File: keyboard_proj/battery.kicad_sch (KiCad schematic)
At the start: 11 parts

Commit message: Tous les schematics vérifiés 1x
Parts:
- removed Q?: FS8205A, SOP65P640X120-8N, symbol SamacSys_Parts:FS8205A
- removed R?: 1k, symbol Device:R
- added BatteryConnector: Conn_01x02, symbol Connector_Generic:Conn_01x02
- added Q?: FS8205A, SOT-23-6L_TCP, symbol 2024-04-15_18-05-36:FS8205A
- added R?: 1k, symbol Device:R
- gave numbers to parts that had none: 2
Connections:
- net GND: now also Q?.3, R?.1
- net at IC?.1 (OD): now also Q?.6
- net at IC?.2 (CS): now also R?.2
- net at IC?.3 (OC): now also Q?.4
- net -: now reaches C?.1, IC?.6 (GND)
- net -: now also BatteryConnector.1 (Pin_1), Q?.1
- net Vbat+ renamed +
- net +: now also BatteryConnector.2 (Pin_2)
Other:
- note added: "Current limiter, checked"
- note added: "Vbat to 3.3V"

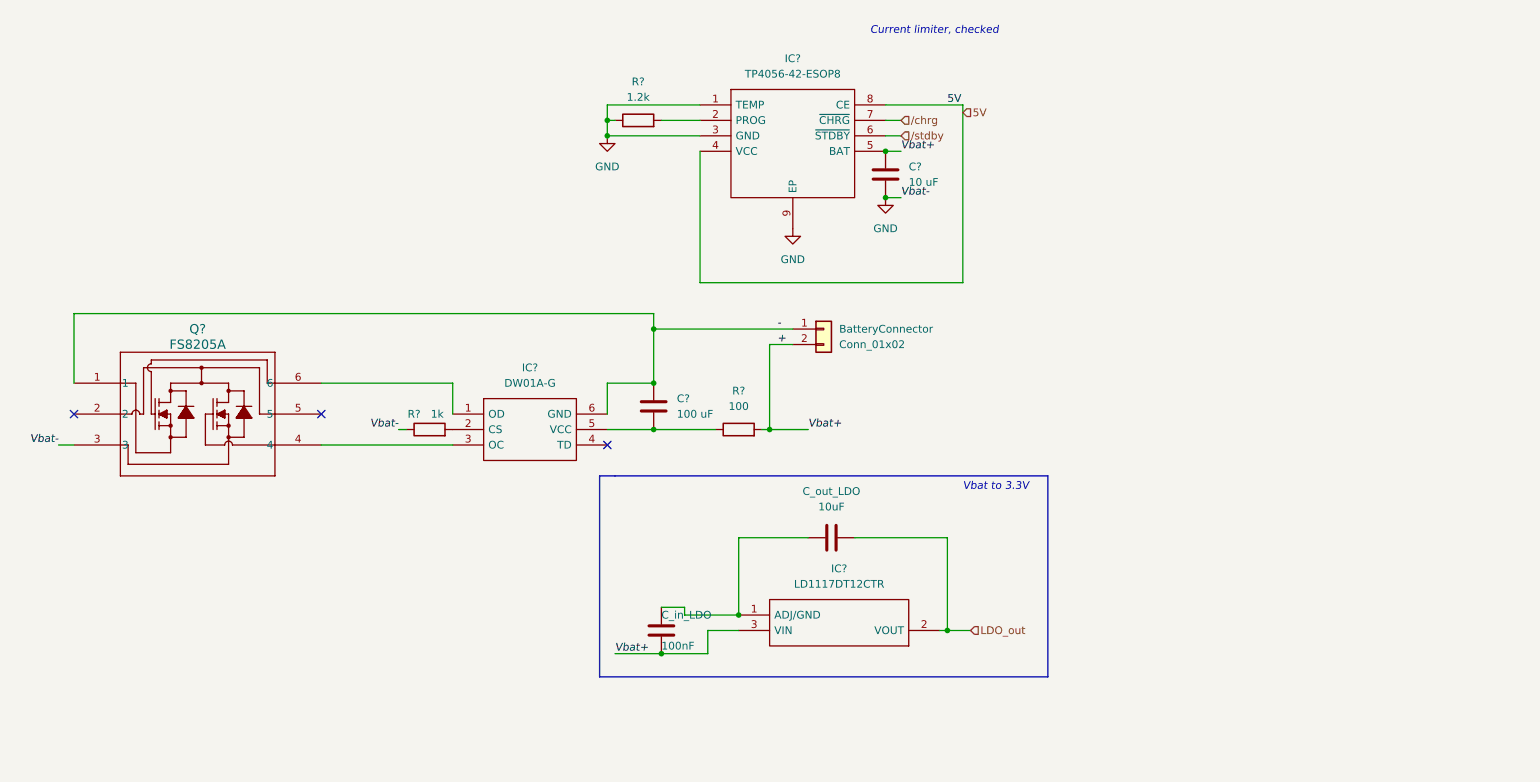
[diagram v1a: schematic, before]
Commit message: Ajout backlight et light sensor (in progress)
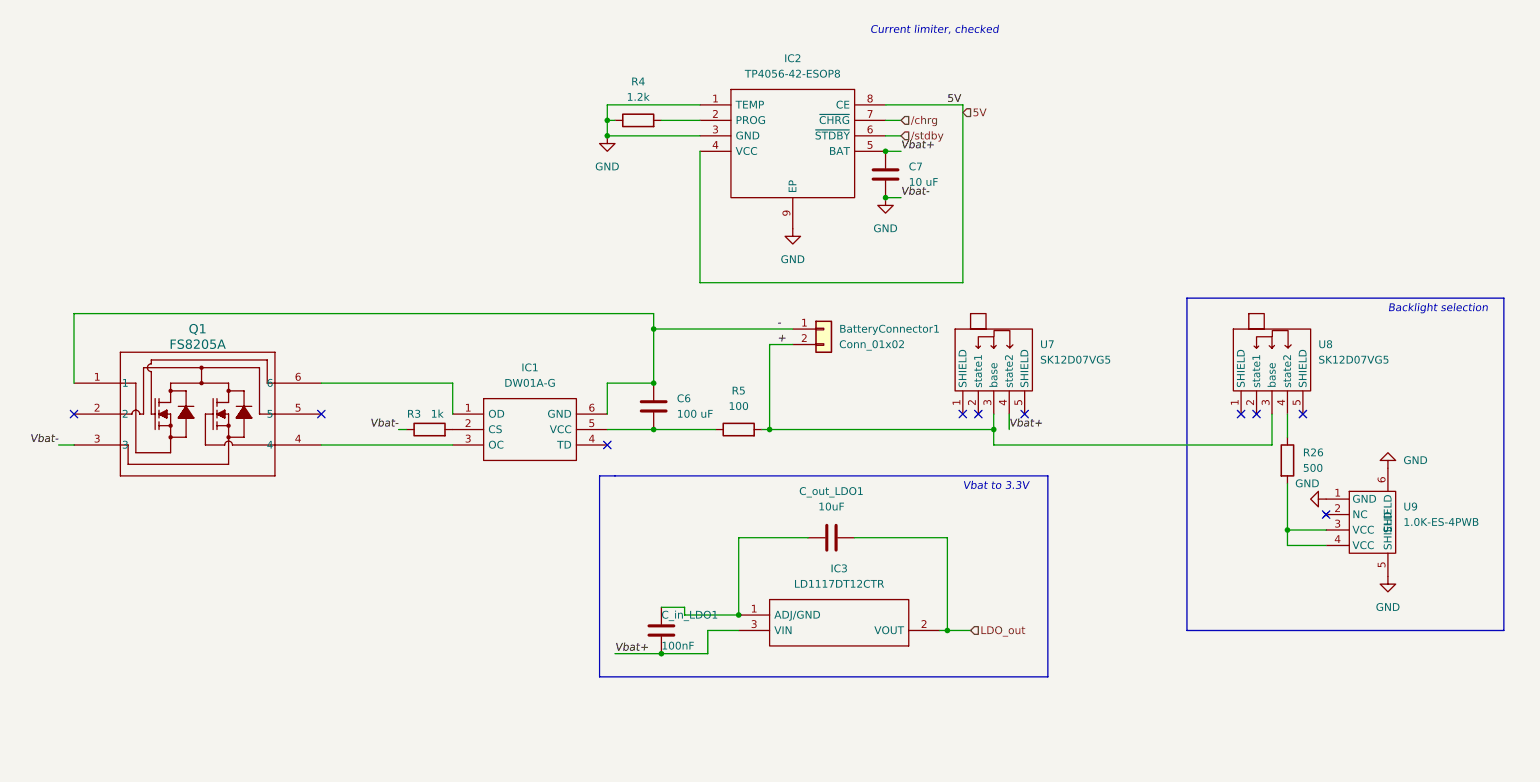
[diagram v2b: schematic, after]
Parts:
- added R26: 500, symbol Device:R
- added U7, U8: SK12D07VG5, symbol My_lib:SK12D07VG5
- added U9: 1.0K-ES-4PWB, symbol My_lib:1.0K-ES-4PWB
- gave numbers to parts that had none: 9
- renumbered BatteryConnector to BatteryConnector1, C_in_LDO to C_in_LDO1, C_out_LDO to C_out_LDO1
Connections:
- net +: now also U7.3 (base), U8.3 (base); no longer C7.1, C_in_LDO1.2, IC2.5 (BAT), IC3.3 (VIN)
- net GND: now also U9.1 (GND), U9.5 (SHIELD), U9.6 (SHIELD)
- new net: R26.1, U8.4 (state2)
- new net: R26.2, U9.3 (VCC), U9.4 (VCC)
- new net Vbat+: C7.1, C_in_LDO1.2, IC2.5 (BAT), IC3.3 (VIN), U7.4 (state2)
- no-connect marks 3 -> 10
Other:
- note added: "Backlight selection"

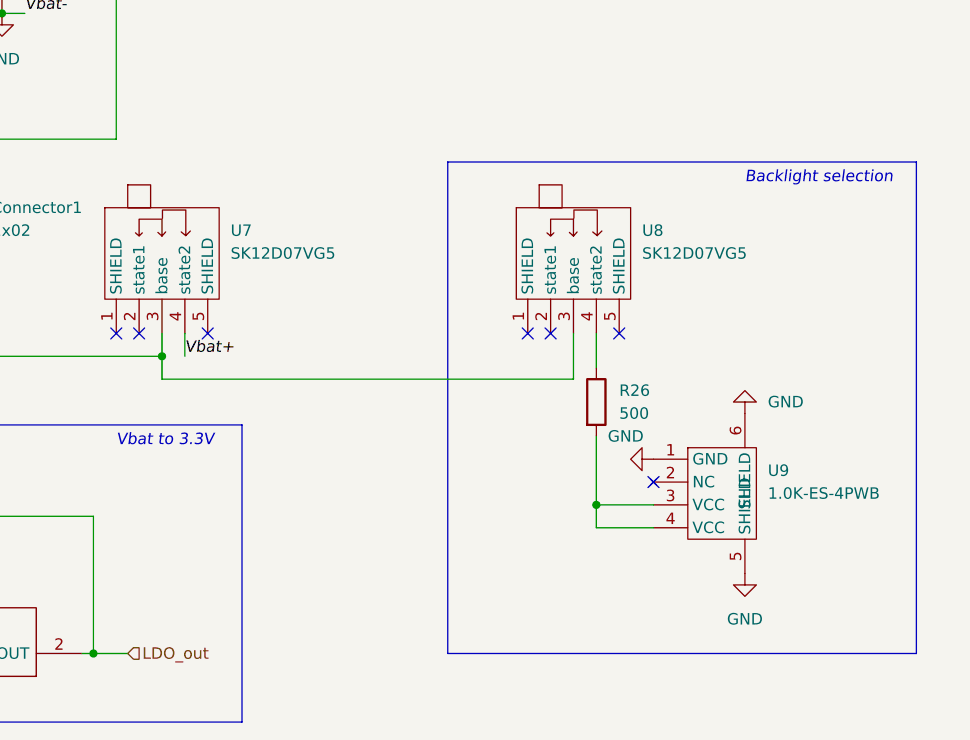
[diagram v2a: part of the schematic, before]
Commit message: Ajout light sensor et controle avec mosfet pour backlight
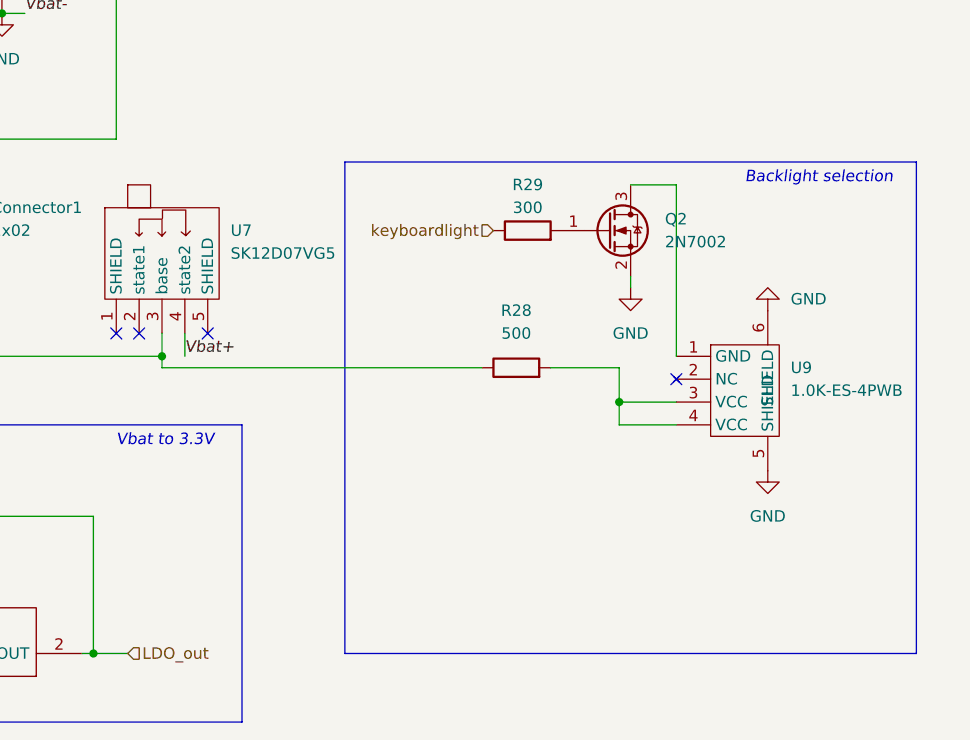
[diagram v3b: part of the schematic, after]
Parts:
- removed R26: 500, symbol Device:R
- removed U8: SK12D07VG5, symbol My_lib:SK12D07VG5
- added Q2: 2N7002, Package_TO_SOT_SMD:SOT-23, symbol Transistor_FET:2N7002
- added R28: 500, symbol Device:R
- added R29: 300, symbol Device:R
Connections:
- net +: now also R28.1
- net GND: now also Q2.2 (S); no longer U9.1 (GND)
- net at U9.3 (VCC), U9.4 (VCC): now also R28.2
- new net: Q2.1 (G), R29.2
- new net: Q2.3 (D), U9.1 (GND)
- new net keyboardlight: R29.1
- no-connect marks 10 -> 7
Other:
- moved on the sheet: U9

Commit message: Ajout des empreintes, il en manque encore
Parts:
- C6, C7, C_in_LDO1, C_out_LDO1: footprint (none) -> Capacitor_SMD:C_0402_1005Metric
- IC1: footprint SOT95P280X135-6N -> FS8205A:SOT-23-6L_TCP-L
- IC2: footprint SOIC127P600X175-9N -> SamacSys_Parts:SOIC127P600X175-9N
- IC3: footprint LD1117DT12CTR -> SamacSys_Parts:LD1117DT12CTR
- Q1: footprint SOT-23-6L_TCP -> FS8205A:SOT-23-6L_TCP
- R28, R29, R3, R4, R5: footprint (none) -> Resistor_SMD:R_0402_1005Metric
- U9: footprint (none) -> SamacSys_Parts:1.0K-ES-4PWB
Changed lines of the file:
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@@
       (effects (font (size 1.27 1.27)) (justify left))
     )
-    (property "Footprint" "" (id 2) (at 177.4952 52.07 0)
+    (property "Footprint" "Capacitor_SMD:C_0402_1005Metric" (id 2) (at 177.4952 52.07 0)
       (effects (font (size 1.27 1.27)) hide)
     )
@@
     (property "Reference" "IC2" (id 0) (at 161.29 29.21 0))
     (property "Value" "TP4056-42-ESOP8" (id 1) (at 161.29 31.75 0))
-    (property "Footprint" "SOIC127P600X175-9N" (id 2) (at 172.72 34.29 0)
+    (property "Footprint" "SamacSys_Parts:SOIC127P600X175-9N" (id 2) (at 172.72 34.29 0)
       (effects (font (size 1.27 1.27)) (justify left) hide)
     )
@@
       (effects (font (size 1.524 1.524)))
     )
-    (property "Footprint" "SOT-23-6L_TCP" (id 2) (at 43.18 82.55 0)
+    (property "Footprint" "FS8205A:SOT-23-6L_TCP" (id 2) (at 43.18 82.55 0)
       (effects (font (size 1.27 1.27) italic) hide)
     )
@@
     (property "Reference" "R3" (id 0) (at 99.06 87.63 90))
     (property "Value" "1k" (id 1) (at 102.87 87.63 90))
-    (property "Footprint" "" (id 2) (at 101.6 91.948 90)
+    (property "Footprint" "Resistor_SMD:R_0402_1005Metric" (id 2) (at 101.6 91.948 90)
       (effects (font (size 1.27 1.27)) hide)
     )
@@
     (property "Reference" "IC1" (id 0) (at 118.11 80.01 0))
     (property "Value" "DW01A-G" (id 1) (at 118.11 82.55 0))
-    (property "Footprint" "SOT95P280X135-6N" (id 2) (at 127 85.09 0)
+    (property "Footprint" "FS8205A:SOT-23-6L_TCP-L" (id 2) (at 127 85.09 0)
       (effects (font (size 1.27 1.27)) (justify left) hide)
     )
@@
     (property "Reference" "R29" (id 0) (at 234.95 71.12 90))
     (property "Value" "300" (id 1) (at 234.95 73.66 90))
-    (property "Footprint" "" (id 2) (at 234.95 77.978 90)
+    (property "Footprint" "Resistor_SMD:R_0402_1005Metric" (id 2) (at 234.95 77.978 90)
       (effects (font (size 1.27 1.27)) hide)
     )
@@
     (property "Reference" "IC3" (id 0) (at 168.91 113.03 0))
     (property "Value" "LD1117DT12CTR" (id 1) (at 168.91 115.57 0))
-    (property "Footprint" "LD1117DT12CTR" (id 2) (at 156.21 125.73 0)
+    (property "Footprint" "SamacSys_Parts:LD1117DT12CTR" (id 2) (at 156.21 125.73 0)
       (effects (font (size 1.27 1.27)) (justify left) hide)
     )
@@
     (property "Reference" "C_out_LDO1" (id 0) (at 167.64 100.33 90))
     (property "Value" "10uF" (id 1) (at 167.64 102.87 90))
-    (property "Footprint" "" (id 2) (at 171.45 106.9848 0)
+    (property "Footprint" "Capacitor_SMD:C_0402_1005Metric" (id 2) (at 171.45 106.9848 0)
       (effects (font (size 1.27 1.27)) hide)
     )
@@
       (effects (font (size 1.27 1.27)) (justify left))
     )
-    (property "Footprint" "" (id 2) (at 140.6652 127 0)
+    (property "Footprint" "Capacitor_SMD:C_0402_1005Metric" (id 2) (at 140.6652 127 0)
       (effects (font (size 1.27 1.27)) hide)
     )
@@
       (effects (font (size 1.27 1.27)) (justify left))
     )
-    (property "Footprint" "" (id 2) (at 259.08 92.71 0)
+    (property "Footprint" "SamacSys_Parts:1.0K-ES-4PWB" (id 2) (at 259.08 92.71 0)
       (effects (font (size 1.27 1.27)) hide)
     )
@@
     (property "Reference" "R28" (id 0) (at 233.68 85.09 90))
     (property "Value" "500" (id 1) (at 233.68 87.63 90))
-    (property "Footprint" "" (id 2) (at 233.68 93.218 90)
+    (property "Footprint" "Resistor_SMD:R_0402_1005Metric" (id 2) (at 233.68 93.218 90)
       (effects (font (size 1.27 1.27)) hide)
     )
@@
     (property "Reference" "R5" (id 0) (at 152.4 83.82 90))
     (property "Value" "100" (id 1) (at 152.4 86.36 90))
-    (property "Footprint" "" (id 2) (at 152.4 91.948 90)
+    (property "Footprint" "Resistor_SMD:R_0402_1005Metric" (id 2) (at 152.4 91.948 90)
       (effects (font (size 1.27 1.27)) hide)
     )
@@
       (effects (font (size 1.27 1.27)) (justify left))
     )
-    (property "Footprint" "" (id 2) (at 139.3952 90.17 0)
+    (property "Footprint" "Capacitor_SMD:C_0402_1005Metric" (id 2) (at 139.3952 90.17 0)
       (effects (font (size 1.27 1.27)) hide)
     )
@@
     (property "Reference" "R4" (id 0) (at 135.89 33.02 90))
     (property "Value" "1.2k" (id 1) (at 135.89 35.56 90))
-    (property "Footprint" "" (id 2) (at 135.89 41.148 90)
-      (effects (font (size 1.27 1.27)) hide)
-    )
+    (property "Footprint" "Resistor_SMD:R_0402_1005Metric" (id 2) (at 135.89 41.148 90)
+      (effects (font (size 1.27 1.27)) hide)
+    )

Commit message: Empreintes finies, besoin de reverifier, disposition des composants sur la carte
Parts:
- BatteryConnector1: footprint (none) -> SamacSys_Parts:Bat_conn
- U7: footprint (none) -> SamacSys_Parts:select_switch
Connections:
- net 5V: now also U7.2 (state1)
- no-connect marks 7 -> 6
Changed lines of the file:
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@@
   (no_connect (at 43.18 87.63))
   (no_connect (at 83.82 87.63))
-  (no_connect (at 191.77 87.63))
   (no_connect (at 130.81 92.71))
   (no_connect (at 189.23 87.63))
@@
     (stroke (width 0) (type default) (color 0 0 0 0))
   )
+  (wire (pts (xy 181.61 88.9) (xy 181.61 87.63))
+    (stroke (width 0) (type default) (color 0 0 0 0))
+  )
   (wire (pts (xy 147.32 123.19) (xy 152.4 123.19))
     (stroke (width 0) (type default) (color 0 0 0 0))
@@
     (stroke (width 0) (type default) (color 0 0 0 0))
   )
+  (wire (pts (xy 191.77 87.63) (xy 191.77 88.9))
+    (stroke (width 0) (type default) (color 0 0 0 0))
+  )
   (polyline (pts (xy 214.63 68.58) (xy 278.13 68.58))
     (stroke (width 0) (type default) (color 0 0 0 0))
@@
     (stroke (width 0) (type default) (color 0 0 0 0))
   )
+  (wire (pts (xy 191.77 88.9) (xy 181.61 88.9))
+    (stroke (width 0) (type default) (color 0 0 0 0))
+  )
   (wire (pts (xy 194.31 90.17) (xy 194.31 87.63))
     (stroke (width 0) (type default) (color 0 0 0 0))
@@
   )
   (label "5V" (at 186.69 36.83 0)
+    (effects (font (size 1.27 1.27)) (justify left bottom))
+  )
+  (label "5V" (at 181.61 87.63 0)
     (effects (font (size 1.27 1.27)) (justify left bottom))
   )
@@
       (effects (font (size 1.27 1.27)) (justify left))
     )
-    (property "Footprint" "" (id 2) (at 194.31 78.74 0)
+    (property "Footprint" "SamacSys_Parts:select_switch" (id 2) (at 194.31 78.74 0)
       (effects (font (size 1.27 1.27)) hide)
     )
@@
       (effects (font (size 1.27 1.27)) (justify left))
     )
-    (property "Footprint" "" (id 2) (at 166.37 73.66 0)
-      (effects (font (size 1.27 1.27)) hide)
-    )
+    (property "Footprint" "SamacSys_Parts:Bat_conn" (id 2) (at 166.37 73.66 0)
+      (effects (font (size 1.27 1.27)) hide)
+    )

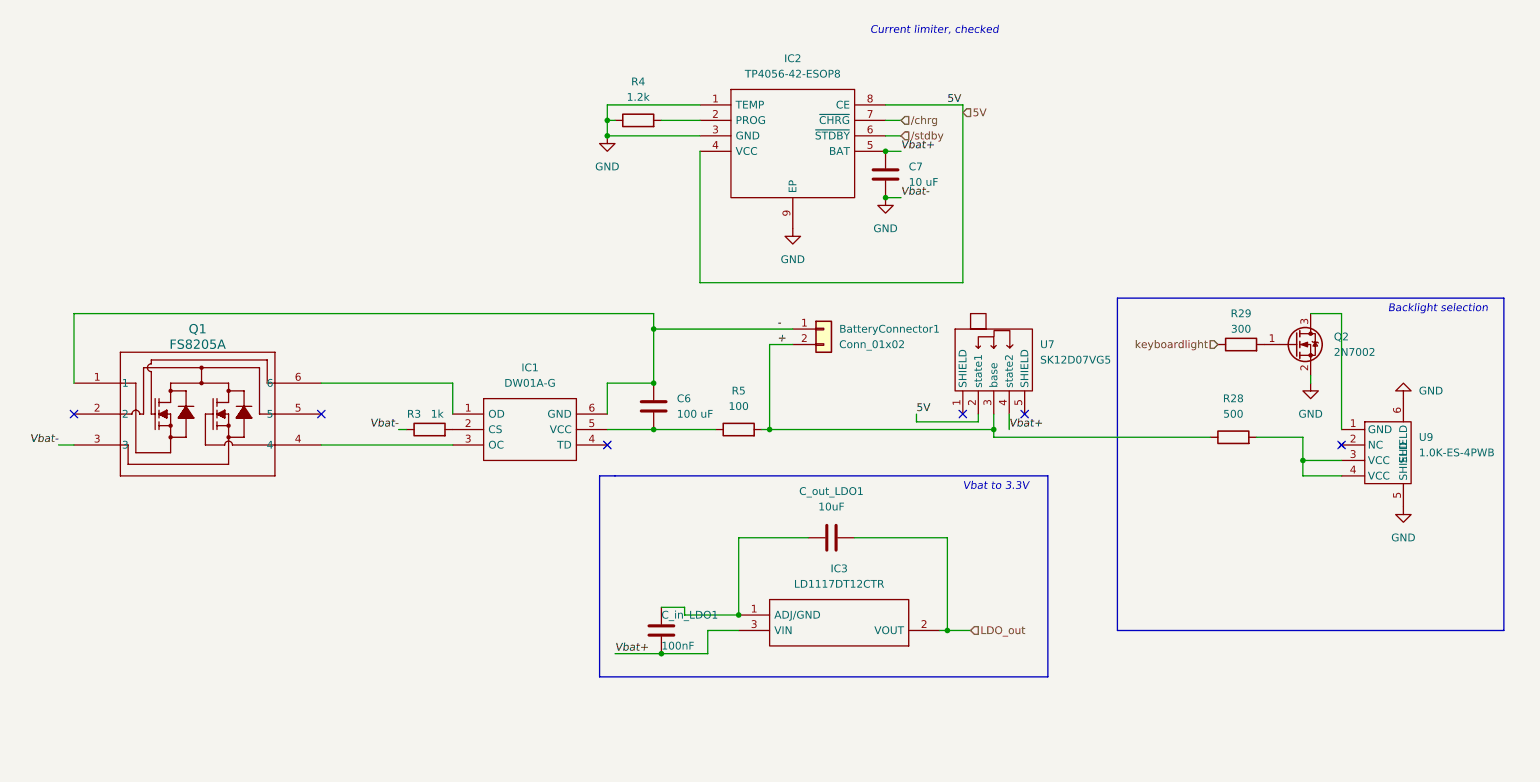
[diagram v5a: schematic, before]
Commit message: passage kicad 7, routing bien avancé
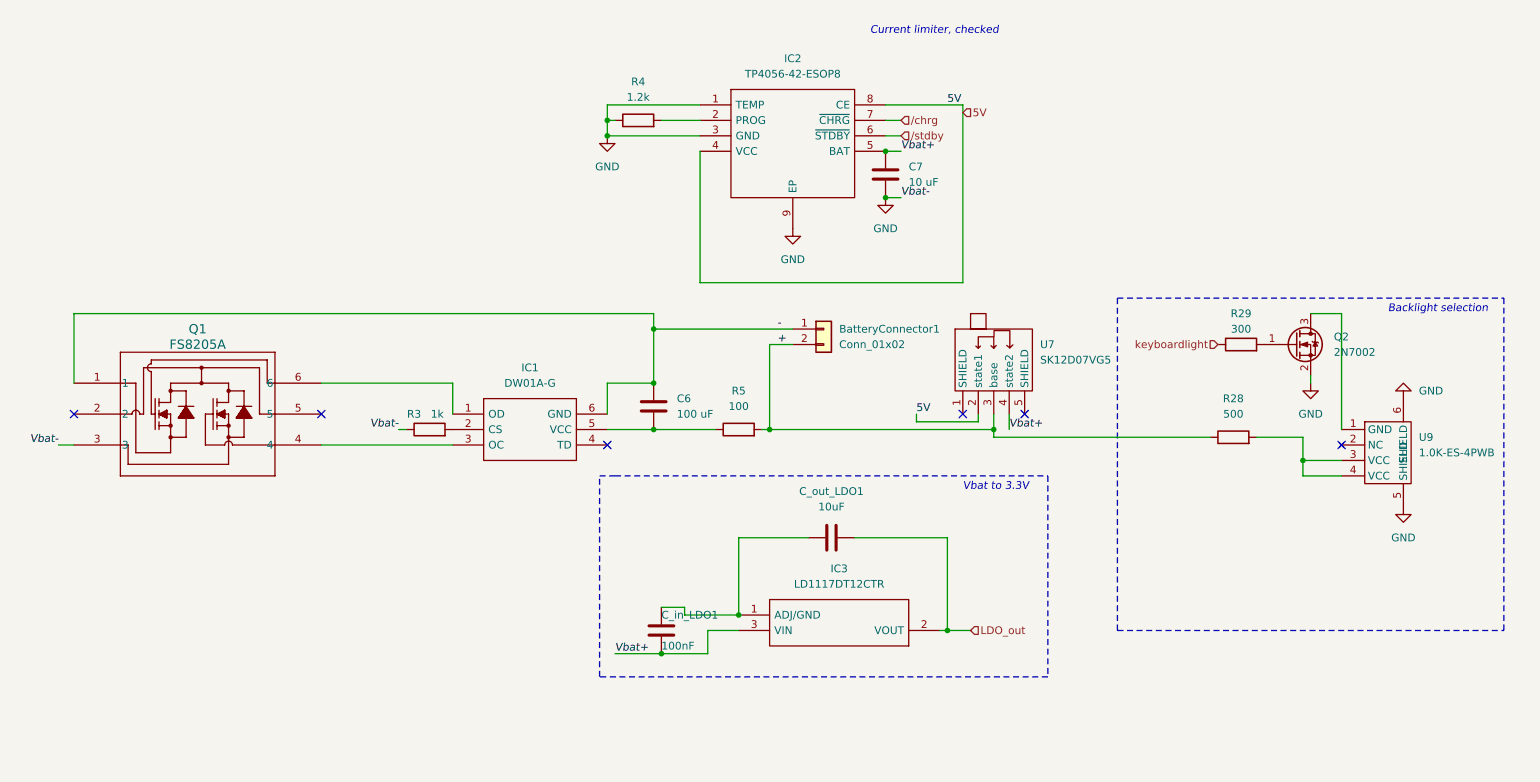
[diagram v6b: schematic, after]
